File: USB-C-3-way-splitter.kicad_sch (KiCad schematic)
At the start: 25 parts, among them J1 USB_C_Receptacle_USB2.0, J2 Conn_01x05_Socket, J3 Conn_01x05_Socket, J4 Conn_01x05_Socket, U1 LM393

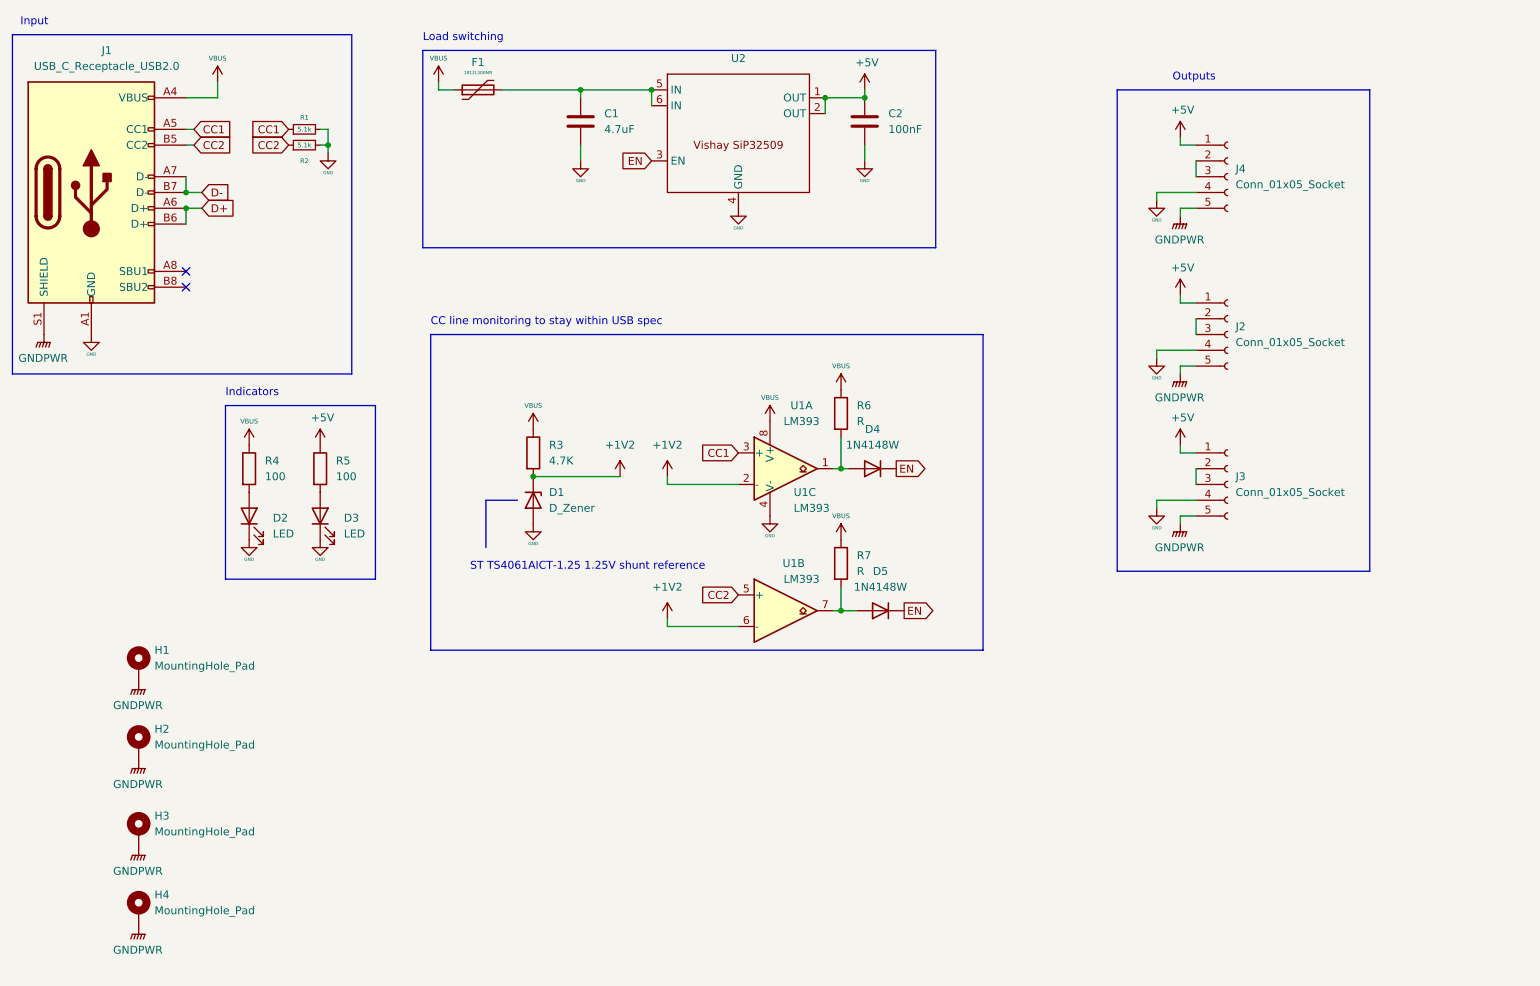
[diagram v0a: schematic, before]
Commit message: Moved everything on the 5v rail to after the fuse
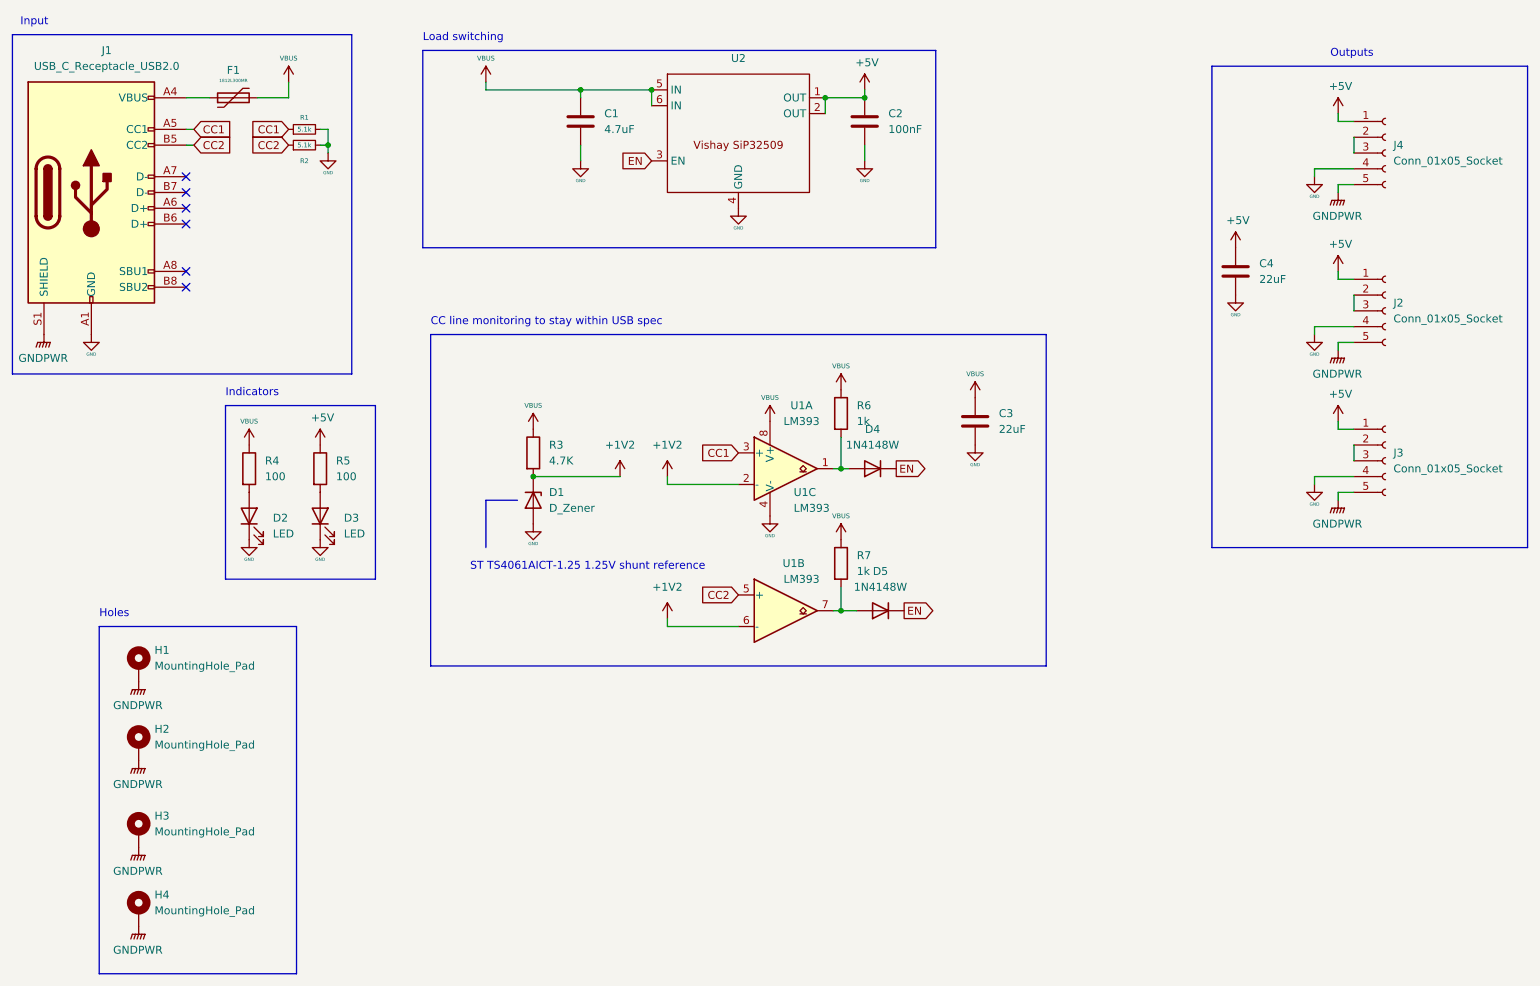
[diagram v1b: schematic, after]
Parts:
- added C3, C4: 22uF, Capacitor_SMD:C_1206_3216Metric_Pad1.33x1.80mm_HandSolder, symbol Device:C
- R6, R7: value R -> 1k
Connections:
- net +5V: now also C4.1
- net GND: now also C3.2, C4.2
- net VBUS: now also C1.1, F1.2, U2.5 (IN), U2.6 (IN), C3.1; no longer F1.1, J1.A4 (VBUS), J1.A9 (VBUS), J1.B4 (VBUS), J1.B9 (VBUS)
- net D+: no longer names the net of J1.A6 (D+)
- net D+: no longer J1.B6 (D+)
- net D-: no longer names the net of J1.A7 (D-)
- net D-: no longer J1.B7 (D-)
- new net: F1.1, J1.A4 (VBUS), J1.A9 (VBUS), J1.B4 (VBUS), J1.B9 (VBUS)
- no-connect marks 2 -> 6
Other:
- note added: "Holes"
- moved on the sheet: F1, J2, J3, J4

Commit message: Open-collectors are inverting ugh. Fixed comparator in schematic.
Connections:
- net +1V2: now also U1.3 (+), U1.5 (+); no longer U1.2 (-), U1.6 (-)
- net CC1: now also U1.2 (-); no longer U1.3 (+)
- net CC2: now also U1.6 (-); no longer U1.5 (+)
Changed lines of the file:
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@@
     (stroke (width 0) (type default))
   )
-  (wire (pts (xy 134.62 92.71) (xy 123.19 92.71))
+  (wire (pts (xy 134.62 87.63) (xy 123.19 87.63))
     (stroke (width 0) (type default))
   )
@@
     (stroke (width 0) (type default))
   )
-  (wire (pts (xy 123.19 92.71) (xy 123.19 91.44))
+  (wire (pts (xy 123.19 87.63) (xy 123.19 86.36))
     (stroke (width 0) (type default))
   )
@@
     (stroke (width 0) (type default))
   )
-  (wire (pts (xy 134.62 115.57) (xy 123.19 115.57))
+  (wire (pts (xy 134.62 110.49) (xy 123.19 110.49))
     (stroke (width 0) (type default))
   )
@@
     (stroke (width 0) (type default))
   )
-  (wire (pts (xy 123.19 115.57) (xy 123.19 114.3))
+  (wire (pts (xy 123.19 110.49) (xy 123.19 109.22))
     (stroke (width 0) (type default))
   )
@@
     )
   )
-  (global_label "CC2" (shape input) (at 134.62 110.49 180) (fields_autoplaced)
+  (global_label "CC2" (shape input) (at 134.62 115.57 180) (fields_autoplaced)
     (effects (font (size 1.27 1.27)) (justify right))
-    (property "Intersheetrefs" "${INTERSHEET_REFS}" (at 127.7902 110.49 0)
+    (property "Intersheetrefs" "${INTERSHEET_REFS}" (at 127.7902 115.57 0)
       (effects (font (size 1.27 1.27)) (justify right) hide)
     )
@@
     )
   )
-  (global_label "CC1" (shape input) (at 134.62 87.63 180) (fields_autoplaced)
+  (global_label "CC1" (shape input) (at 134.62 92.71 180) (fields_autoplaced)
     (effects (font (size 1.27 1.27)) (justify right))
-    (property "Intersheetrefs" "${INTERSHEET_REFS}" (at 127.7902 87.63 0)
+    (property "Intersheetrefs" "${INTERSHEET_REFS}" (at 127.7902 92.71 0)
       (effects (font (size 1.27 1.27)) (justify right) hide)
     )
@@
     )
   )
-  (symbol (lib_id "power:+1V2") (at 123.19 91.44 0) (unit 1)
+  (symbol (lib_id "power:+1V2") (at 123.19 86.36 0) (unit 1)
     (in_bom yes) (on_board yes) (dnp no) (fields_autoplaced)
-    (property "Reference" "#PWR023" (at 123.19 95.25 0)
-      (effects (font (size 1.27 1.27)) hide)
-    )
-    (property "Value" "+1V2" (at 123.19 86.36 0)
-      (effects (font (size 1.27 1.27)))
-    )
-    (property "Footprint" "" (at 123.19 91.44 0)
-      (effects (font (size 1.27 1.27)) hide)
-    )
-    (property "Datasheet" "" (at 123.19 91.44 0)
+    (property "Reference" "#PWR023" (at 123.19 90.17 0)
+      (effects (font (size 1.27 1.27)) hide)
+    )
+    (property "Value" "+1V2" (at 123.19 81.28 0)
+      (effects (font (size 1.27 1.27)))
+    )
+    (property "Footprint" "" (at 123.19 86.36 0)
+      (effects (font (size 1.27 1.27)) hide)
+    )
+    (property "Datasheet" "" (at 123.19 86.36 0)
       (effects (font (size 1.27 1.27)) hide)
     )
@@
     )
   )
-  (symbol (lib_id "power:+1V2") (at 123.19 114.3 0) (unit 1)
+  (symbol (lib_id "power:+1V2") (at 123.19 109.22 0) (unit 1)
     (in_bom yes) (on_board yes) (dnp no) (fields_autoplaced)
-    (property "Reference" "#PWR024" (at 123.19 118.11 0)
-      (effects (font (size 1.27 1.27)) hide)
-    )
-    (property "Value" "+1V2" (at 123.19 109.22 0)
-      (effects (font (size 1.27 1.27)))
-    )
-    (property "Footprint" "" (at 123.19 114.3 0)
-      (effects (font (size 1.27 1.27)) hide)
-    )
-    (property "Datasheet" "" (at 123.19 114.3 0)
-      (effects (font (size 1.27 1.27)) hide)
-    )
+    (property "Reference" "#PWR024" (at 123.19 113.03 0)
+      (effects (font (size 1.27 1.27)) hide)
+    )
+    (property "Value" "+1V2" (at 123.19 104.14 0)
+      (effects (font (size 1.27 1.27)))
+    )
+    (property "Footprint" "" (at 123.19 109.22 0)
+      (effects (font (size 1.27 1.27)) hide)
+    )
+    (property "Datasheet" "" (at 123.19 109.22 0)
+      (effects (font (size 1.27 1.27)) hide)
+    )

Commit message: Never mind misunderstood the LM393M's behavior
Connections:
- net +1V2: now also U1.2 (-), U1.6 (-); no longer U1.3 (+), U1.5 (+)
- net CC1: now also U1.3 (+); no longer U1.2 (-)
- net CC2: now also U1.5 (+); no longer U1.6 (-)
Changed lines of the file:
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@@
     (stroke (width 0) (type default))
   )
-  (wire (pts (xy 134.62 87.63) (xy 123.19 87.63))
+  (wire (pts (xy 134.62 92.71) (xy 123.19 92.71))
     (stroke (width 0) (type default))
   )
@@
     (stroke (width 0) (type default))
   )
-  (wire (pts (xy 123.19 87.63) (xy 123.19 86.36))
+  (wire (pts (xy 123.19 92.71) (xy 123.19 91.44))
     (stroke (width 0) (type default))
   )
@@
     (stroke (width 0) (type default))
   )
-  (wire (pts (xy 134.62 110.49) (xy 123.19 110.49))
+  (wire (pts (xy 134.62 115.57) (xy 123.19 115.57))
     (stroke (width 0) (type default))
   )
@@
     (stroke (width 0) (type default))
   )
-  (wire (pts (xy 123.19 110.49) (xy 123.19 109.22))
+  (wire (pts (xy 123.19 115.57) (xy 123.19 114.3))
     (stroke (width 0) (type default))
   )
@@
     )
   )
-  (global_label "CC2" (shape input) (at 134.62 115.57 180) (fields_autoplaced)
+  (global_label "CC2" (shape input) (at 134.62 110.49 180) (fields_autoplaced)
     (effects (font (size 1.27 1.27)) (justify right))
-    (property "Intersheetrefs" "${INTERSHEET_REFS}" (at 127.7902 115.57 0)
+    (property "Intersheetrefs" "${INTERSHEET_REFS}" (at 127.7902 110.49 0)
       (effects (font (size 1.27 1.27)) (justify right) hide)
     )
@@
     )
   )
-  (global_label "CC1" (shape input) (at 134.62 92.71 180) (fields_autoplaced)
+  (global_label "CC1" (shape input) (at 134.62 87.63 180) (fields_autoplaced)
     (effects (font (size 1.27 1.27)) (justify right))
-    (property "Intersheetrefs" "${INTERSHEET_REFS}" (at 127.7902 92.71 0)
+    (property "Intersheetrefs" "${INTERSHEET_REFS}" (at 127.7902 87.63 0)
       (effects (font (size 1.27 1.27)) (justify right) hide)
     )
@@
     )
   )
-  (symbol (lib_id "power:+1V2") (at 123.19 86.36 0) (unit 1)
+  (symbol (lib_id "power:+1V2") (at 123.19 91.44 0) (unit 1)
     (in_bom yes) (on_board yes) (dnp no) (fields_autoplaced)
-    (property "Reference" "#PWR023" (at 123.19 90.17 0)
-      (effects (font (size 1.27 1.27)) hide)
-    )
-    (property "Value" "+1V2" (at 123.19 81.28 0)
-      (effects (font (size 1.27 1.27)))
-    )
-    (property "Footprint" "" (at 123.19 86.36 0)
-      (effects (font (size 1.27 1.27)) hide)
-    )
-    (property "Datasheet" "" (at 123.19 86.36 0)
+    (property "Reference" "#PWR023" (at 123.19 95.25 0)
+      (effects (font (size 1.27 1.27)) hide)
+    )
+    (property "Value" "+1V2" (at 123.19 86.36 0)
+      (effects (font (size 1.27 1.27)))
+    )
+    (property "Footprint" "" (at 123.19 91.44 0)
+      (effects (font (size 1.27 1.27)) hide)
+    )
+    (property "Datasheet" "" (at 123.19 91.44 0)
       (effects (font (size 1.27 1.27)) hide)
     )
@@
     )
   )
-  (symbol (lib_id "power:+1V2") (at 123.19 109.22 0) (unit 1)
+  (symbol (lib_id "power:+1V2") (at 123.19 114.3 0) (unit 1)
     (in_bom yes) (on_board yes) (dnp no) (fields_autoplaced)
-    (property "Reference" "#PWR024" (at 123.19 113.03 0)
-      (effects (font (size 1.27 1.27)) hide)
-    )
-    (property "Value" "+1V2" (at 123.19 104.14 0)
-      (effects (font (size 1.27 1.27)))
-    )
-    (property "Footprint" "" (at 123.19 109.22 0)
-      (effects (font (size 1.27 1.27)) hide)
-    )
-    (property "Datasheet" "" (at 123.19 109.22 0)
-      (effects (font (size 1.27 1.27)) hide)
-    )
+    (property "Reference" "#PWR024" (at 123.19 118.11 0)
+      (effects (font (size 1.27 1.27)) hide)
+    )
+    (property "Value" "+1V2" (at 123.19 109.22 0)
+      (effects (font (size 1.27 1.27)))
+    )
+    (property "Footprint" "" (at 123.19 114.3 0)
+      (effects (font (size 1.27 1.27)) hide)
+    )
+    (property "Datasheet" "" (at 123.19 114.3 0)
+      (effects (font (size 1.27 1.27)) hide)
+    )

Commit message: Design is done maybe?
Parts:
- added C5: 100nF, Capacitor_SMD:C_0805_2012Metric_Pad1.18x1.45mm_HandSolder, symbol Device:C
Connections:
- net +1V2: now also C5.1
- net GND: now also C5.2
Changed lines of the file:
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@@
   (junction (at 68.58 38.1) (diameter 0) (color 0 0 0 0)
+  )
+  (junction (at 115.57 91.44) (diameter 0) (color 0 0 0 0)
   )
   (junction (at 154.94 30.48) (diameter 0) (color 0 0 0 0)
@@
     )
   )
+  (symbol (lib_id "Device:C") (at 115.57 95.25 0) (unit 1)
+    (in_bom yes) (on_board yes) (dnp no) (fields_autoplaced)
+    (property "Reference" "C5" (at 119.38 93.98 0)
+      (effects (font (size 1.27 1.27)) (justify left))
+    )
+    (property "Value" "100nF" (at 119.38 96.52 0)
+      (effects (font (size 1.27 1.27)) (justify left))
+    )
+    (property "Footprint" "Capacitor_SMD:C_0805_2012Metric_Pad1.18x1.45mm_HandSolder" (at 116.5352 99.06 0)
+      (effects (font (size 1.27 1.27)) hide)
+    )
+    (property "Datasheet" "~" (at 115.57 95.25 0)
+      (effects (font (size 1.27 1.27)) hide)
+    )
+    (pin "1")
+    (pin "2")
+    (instances
+      (project "USB-C-3-way-splitter"
+        (path "/49b03f2e-4a93-4c4e-8d95-13775b5bcebc"
+          (reference "C5") (unit 1)
+        )
+      )
+    )
+  )
   (symbol (lib_id "Device:C") (at 172.72 82.55 0) (unit 1)
     (in_bom yes) (on_board yes) (dnp no) (fields_autoplaced)
@@
         )
       )
+    )
+  )
+  (symbol (lib_id "power:GND") (at 115.57 99.06 0) (unit 1)
+    (in_bom yes) (on_board yes) (dnp no)
+    (property "Reference" "#PWR036" (at 115.57 105.41 0)
+      (effects (font (size 1.27 1.27)) hide)
+    )
+    (property "Value" "GND" (at 115.57 102.235 0)
+      (effects (font (size 0.508 0.508)))
+    )
+    (property "Footprint" "" (at 115.57 99.06 0)
+      (effects (font (size 1.27 1.27)) hide)
+    )
+    (property "Datasheet" "" (at 115.57 99.06 0)
+      (effects (font (size 1.27 1.27)) hide)
+    )
+    (pin "1")
+    (instances
+      (project "USB-C-3-way-splitter"
+        (path "/49b03f2e-4a93-4c4e-8d95-13775b5bcebc"
+          (reference "#PWR036") (unit 1)
+        )
+      )

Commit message: Added JLCPCB tooling holes
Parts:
- added H5, H6, H7: MountingHole, USB-C-3-way-splitter-footprints:JLCPCB-tooling-hole, symbol Mechanical:MountingHole
- U2: value ~ -> SiP32509
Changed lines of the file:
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@@
-    (stroke (width 0) (type default))
-  )
-  (polyline (pts (xy 31.75 115.57) (xy 63.5 115.57))
     (stroke (width 0) (type default))
   )
@@
   )
   (wire (pts (xy 149.86 90.17) (xy 151.13 90.17))
-    (stroke (width 0) (type default))
-  )
-  (polyline (pts (xy 31.75 115.57) (xy 31.75 171.45))
     (stroke (width 0) (type default))
   )
@@
     (stroke (width 0) (type solid))
   )
-  (polyline (pts (xy 63.5 171.45) (xy 31.75 171.45))
-    (stroke (width 0) (type default))
-  )
   (wire (pts (xy 231.14 59.69) (xy 231.14 58.42))
     (stroke (width 0) (type default))
@@
   )
   (polyline (pts (xy 83.82 22.86) (xy 166.37 22.86))
-    (stroke (width 0) (type default))
-  )
-  (polyline (pts (xy 63.5 115.57) (xy 63.5 171.45))
     (stroke (width 0) (type default))
   )
@@
       (effects (font (size 1.27 1.27)))
     )
-    (property "Value" "~" (at 134.62 35.56 0)
+    (property "Value" "SiP32509" (at 134.62 35.56 0)
       (effects (font (size 1.27 1.27)))
     )
@@
         (path "/49b03f2e-4a93-4c4e-8d95-13775b5bcebc"
           (reference "#PWR025") (unit 1)
+        )
+      )
+    )
+  )
+  (symbol (lib_id "Mechanical:MountingHole") (at 64.77 147.32 0) (unit 1)
+    (in_bom yes) (on_board yes) (dnp no) (fields_autoplaced)
+    (property "Reference" "H7" (at 67.31 146.05 0)
+      (effects (font (size 1.27 1.27)) (justify left))
+    )
+    (property "Value" "MountingHole" (at 67.31 148.59 0)
+      (effects (font (size 1.27 1.27)) (justify left))
+    )
+    (property "Footprint" "USB-C-3-way-splitter-footprints:JLCPCB-tooling-hole" (at 64.77 147.32 0)
+      (effects (font (size 1.27 1.27)) hide)
+    )
+    (property "Datasheet" "~" (at 64.77 147.32 0)
+      (effects (font (size 1.27 1.27)) hide)
+    )
+    (instances
+      (project "USB-C-3-way-splitter"
+        (path "/49b03f2e-4a93-4c4e-8d95-13775b5bcebc"
+          (reference "H7") (unit 1)
         )
       )
@@
     )
   )
+  (symbol (lib_id "Mechanical:MountingHole") (at 64.77 120.65 0) (unit 1)
+    (in_bom yes) (on_board yes) (dnp no) (fields_autoplaced)
+    (property "Reference" "H5" (at 67.31 119.38 0)
+      (effects (font (size 1.27 1.27)) (justify left))
+    )
+    (property "Value" "MountingHole" (at 67.31 121.92 0)
+      (effects (font (size 1.27 1.27)) (justify left))
+    )
+    (property "Footprint" "USB-C-3-way-splitter-footprints:JLCPCB-tooling-hole" (at 64.77 120.65 0)
+      (effects (font (size 1.27 1.27)) hide)
+    )
+    (property "Datasheet" "~" (at 64.77 120.65 0)
+      (effects (font (size 1.27 1.27)) hide)
+    )
+    (instances
+      (project "USB-C-3-way-splitter"
+        (path "/49b03f2e-4a93-4c4e-8d95-13775b5bcebc"
+          (reference "H5") (unit 1)
+        )
+      )
+    )
+  )
   (symbol (lib_id "Device:C") (at 115.57 95.25 0) (unit 1)
     (in_bom yes) (on_board yes) (dnp no) (fields_autoplaced)
@@
         )
       )
+    )
+  )
+  (symbol (lib_id "Mechanical:MountingHole") (at 64.77 133.35 0) (unit 1)
+    (in_bom yes) (on_board yes) (dnp no) (fields_autoplaced)
+    (property "Reference" "H6" (at 67.31 132.08 0)
+      (effects (font (size 1.27 1.27)) (justify left))
+    )
+    (property "Value" "MountingHole" (at 67.31 134.62 0)
+      (effects (font (size 1.27 1.27)) (justify left))
+    )
+    (property "Footprint" "USB-C-3-way-splitter-footprints:JLCPCB-tooling-hole" (at 64.77 133.35 0)
+      (effects (font (size 1.27 1.27)) hide)
+    )
+    (property "Datasheet" "~" (at 64.77 133.35 0)
+      (effects (font (size 1.27 1.27)) hide)
+    )
+    (instances
+      (project "USB-C-3-way-splitter"
+        (path "/49b03f2e-4a93-4c4e-8d95-13775b5bcebc"
+          (reference "H6") (unit 1)
+        )
+      )
